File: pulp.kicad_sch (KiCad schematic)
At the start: 0 parts

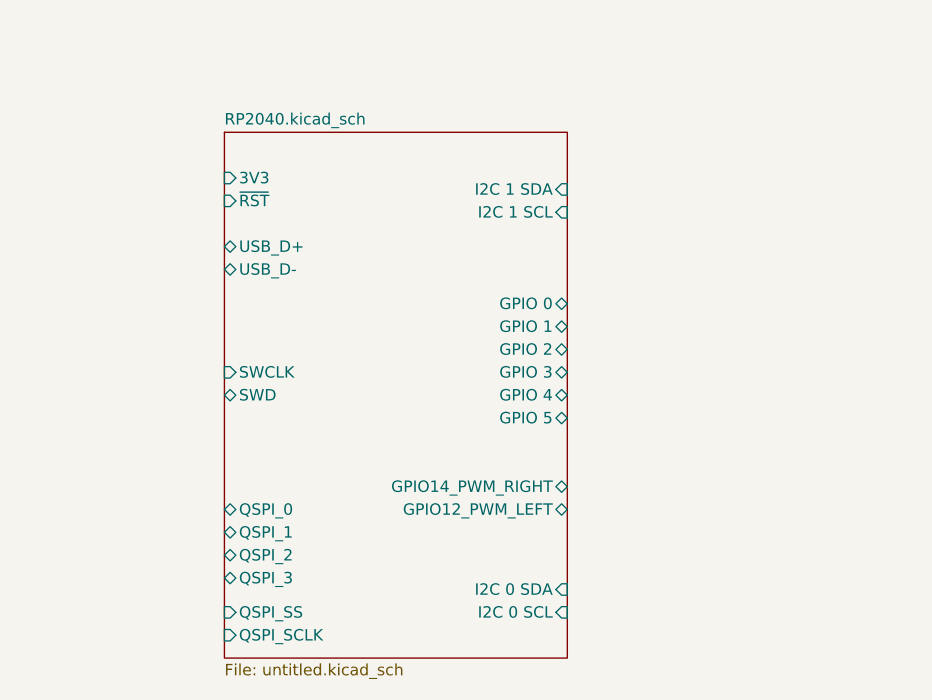
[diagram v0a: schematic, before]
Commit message: adds QMC5883L
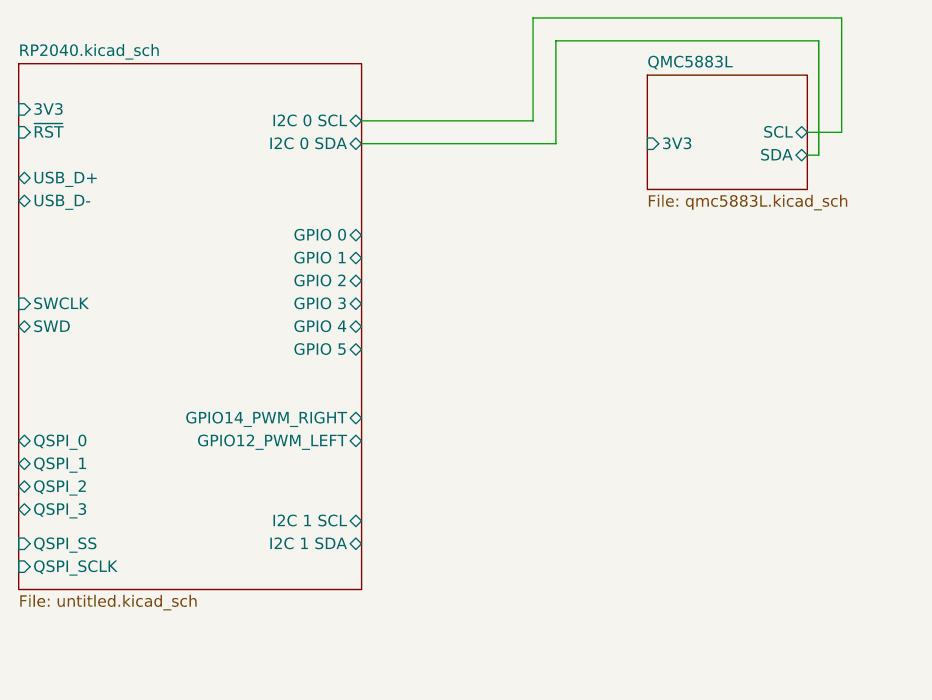
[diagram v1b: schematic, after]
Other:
- added sheet QMC5883L (qmc5883L.kicad_sch)
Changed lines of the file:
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@@
 (kicad_sch (version 20230121) (generator eeschema)
   (paper "A4")
-  (sheet (at 55.88 29.21) (size 38.1 58.42) (fields_autoplaced)
+  (wire (pts (xy 92.71 30.48) (xy 92.71 19.05))
+    (stroke (width 0) (type default))
+  )
+  (wire (pts (xy 121.92 31.75) (xy 120.65 31.75))
+    (stroke (width 0) (type default))
+  )
+  (wire (pts (xy 71.12 27.94) (xy 90.17 27.94))
+    (stroke (width 0) (type default))
+  )
+  (wire (pts (xy 121.92 19.05) (xy 121.92 31.75))
+    (stroke (width 0) (type default))
+  )
+  (wire (pts (xy 124.46 29.21) (xy 120.65 29.21))
+    (stroke (width 0) (type default))
+  )
+  (wire (pts (xy 90.17 27.94) (xy 90.17 16.51))
+    (stroke (width 0) (type default))
+  )
+  (wire (pts (xy 124.46 16.51) (xy 124.46 29.21))
+    (stroke (width 0) (type default))
+  )
+  (wire (pts (xy 90.17 16.51) (xy 124.46 16.51))
+    (stroke (width 0) (type default))
+  )
+  (wire (pts (xy 71.12 30.48) (xy 92.71 30.48))
+    (stroke (width 0) (type default))
+  )
+  (wire (pts (xy 92.71 19.05) (xy 121.92 19.05))
+    (stroke (width 0) (type default))
+  )
+  (sheet (at 33.02 21.59) (size 38.1 58.42) (fields_autoplaced)
     (stroke (width 0.1524) (type solid))
     (fill (color 0 0 0 0.0000))
-    (property "Sheetname" "RP2040.kicad_sch" (at 55.88 28.4984 0)
+    (property "Sheetname" "RP2040.kicad_sch" (at 33.02 20.8784 0)
       (effects (font (size 1.27 1.27)) (justify left bottom))
     )
-    (property "Sheetfile" "untitled.kicad_sch" (at 55.88 88.2146 0)
+    (property "Sheetfile" "untitled.kicad_sch" (at 33.02 80.5946 0)
       (effects (font (size 1.27 1.27)) (justify left top))
     )
-    (pin "3V3" input (at 55.88 34.29 180)
+    (pin "3V3" input (at 33.02 26.67 180)
       (effects (font (size 1.27 1.27)) (justify left))
     )
-    (pin "~{RST}" input (at 55.88 36.83 180)
+    (pin "~{RST}" input (at 33.02 29.21 180)
       (effects (font (size 1.27 1.27)) (justify left))
     )
-    (pin "SWD" bidirectional (at 55.88 58.42 180)
+    (pin "SWD" bidirectional (at 33.02 50.8 180)
       (effects (font (size 1.27 1.27)) (justify left))
     )
-    (pin "SWCLK" input (at 55.88 55.88 180)
+    (pin "SWCLK" input (at 33.02 48.26 180)
       (effects (font (size 1.27 1.27)) (justify left))
     )
-    (pin "QSPI_SCLK" input (at 55.88 85.09 180)
+    (pin "QSPI_SCLK" input (at 33.02 77.47 180)
       (effects (font (size 1.27 1.27)) (justify left))
     )
-    (pin "USB_D-" bidirectional (at 55.88 44.45 180)
+    (pin "USB_D-" bidirectional (at 33.02 36.83 180)
       (effects (font (size 1.27 1.27)) (justify left))
     )
-    (pin "QSPI_SS" input (at 55.88 82.55 180)
+    (pin "QSPI_SS" input (at 33.02 74.93 180)
       (effects (font (size 1.27 1.27)) (justify left))
     )
-    (pin "USB_D+" bidirectional (at 55.88 41.91 180)
+    (pin "USB_D+" bidirectional (at 33.02 34.29 180)
       (effects (font (size 1.27 1.27)) (justify left))
     )
-    (pin "QSPI_3" bidirectional (at 55.88 78.74 180)
+    (pin "QSPI_3" bidirectional (at 33.02 71.12 180)
       (effects (font (size 1.27 1.27)) (justify left))
     )
-    (pin "QSPI_2" bidirectional (at 55.88 76.2 180)
+    (pin "QSPI_2" bidirectional (at 33.02 68.58 180)
       (effects (font (size 1.27 1.27)) (justify left))
     )
-    (pin "QSPI_1" bidirectional (at 55.88 73.66 180)
+    (pin "QSPI_1" bidirectional (at 33.02 66.04 180)
       (effects (font (size 1.27 1.27)) (justify left))
     )
-    (pin "QSPI_0" bidirectional (at 55.88 71.12 180)
+    (pin "QSPI_0" bidirectional (at 33.02 63.5 180)
       (effects (font (size 1.27 1.27)) (justify left))
     )
-    (pin "I2C 1 SDA" input (at 93.98 35.56 0)
+    (pin "GPIO 4" bidirectional (at 71.12 50.8 0)
       (effects (font (size 1.27 1.27)) (justify right))
     )
-    (pin "I2C 1 SCL" input (at 93.98 38.1 0)
+    (pin "GPIO 1" bidirectional (at 71.12 43.18 0)
       (effects (font (size 1.27 1.27)) (justify right))
     )
-    (pin "I2C 0 SDA" input (at 93.98 80.01 0)
+    (pin "GPIO 2" bidirectional (at 71.12 45.72 0)
       (effects (font (size 1.27 1.27)) (justify right))
     )
-    (pin "I2C 0 SCL" input (at 93.98 82.55 0)
+    (pin "GPIO 3" bidirectional (at 71.12 48.26 0)
       (effects (font (size 1.27 1.27)) (justify right))
     )
-    (pin "GPIO 4" bidirectional (at 93.98 58.42 0)
+    (pin "GPIO 5" bidirectional (at 71.12 53.34 0)
       (effects (font (size 1.27 1.27)) (justify right))
     )
-    (pin "GPIO 1" bidirectional (at 93.98 50.8 0)
+    (pin "GPIO 0" bidirectional (at 71.12 40.64 0)
       (effects (font (size 1.27 1.27)) (justify right))
     )
-    (pin "GPIO 2" bidirectional (at 93.98 53.34 0)
+    (pin "GPIO14_PWM_RIGHT" bidirectional (at 71.12 60.96 0)
       (effects (font (size 1.27 1.27)) (justify right))
     )
-    (pin "GPIO 3" bidirectional (at 93.98 55.88 0)
+    (pin "GPIO12_PWM_LEFT" bidirectional (at 71.12 63.5 0)
       (effects (font (size 1.27 1.27)) (justify right))
     )
-    (pin "GPIO 5" bidirectional (at 93.98 60.96 0)
+    (pin "I2C 0 SCL" bidirectional (at 71.12 27.94 0)
       (effects (font (size 1.27 1.27)) (justify right))
     )
-    (pin "GPIO 0" bidirectional (at 93.98 48.26 0)
+    (pin "I2C 1 SDA" bidirectional (at 71.12 74.93 0)
       (effects (font (size 1.27 1.27)) (justify right))
     )
-    (pin "GPIO14_PWM_RIGHT" bidirectional (at 93.98 68.58 0)
+    (pin "I2C 0 SDA" bidirectional (at 71.12 30.48 0)
       (effects (font (size 1.27 1.27)) (justify right))
     )
-    (pin "GPIO12_PWM_LEFT" bidirectional (at 93.98 71.12 0)
+    (pin "I2C 1 SCL" bidirectional (at 71.12 72.39 0)
       (effects (font (size 1.27 1.27)) (justify right))
     )
@@
       )
     )
+  )
+  (sheet (at 102.87 22.86) (size 17.78 12.7) (fields_autoplaced)
+    (stroke (width 0.1524) (type solid))
+    (fill (color 0 0 0 0.0000))
+    (property "Sheetname" "QMC5883L" (at 102.87 22.1484 0)
+      (effects (font (size 1.27 1.27)) (justify left bottom))
+    )
+    (property "Sheetfile" "qmc5883L.kicad_sch" (at 102.87 36.1446 0)
+      (effects (font (size 1.27 1.27)) (justify left top))
+    )
+    (pin "3V3" input (at 102.87 30.48 180)
+      (effects (font (size 1.27 1.27)) (justify left))
+    )
+    (pin "SCL" bidirectional (at 120.65 29.21 0)
+      (effects (font (size 1.27 1.27)) (justify right))
+    )
+    (pin "SDA" bidirectional (at 120.65 31.75 0)
+      (effects (font (size 1.27 1.27)) (justify right))
+    )
+    (instances
+      (project "pulp"
+        (path "/1ed16f22-2fbd-4fb8-a593-4becb783d131" (page "3"))
+      )
+    )

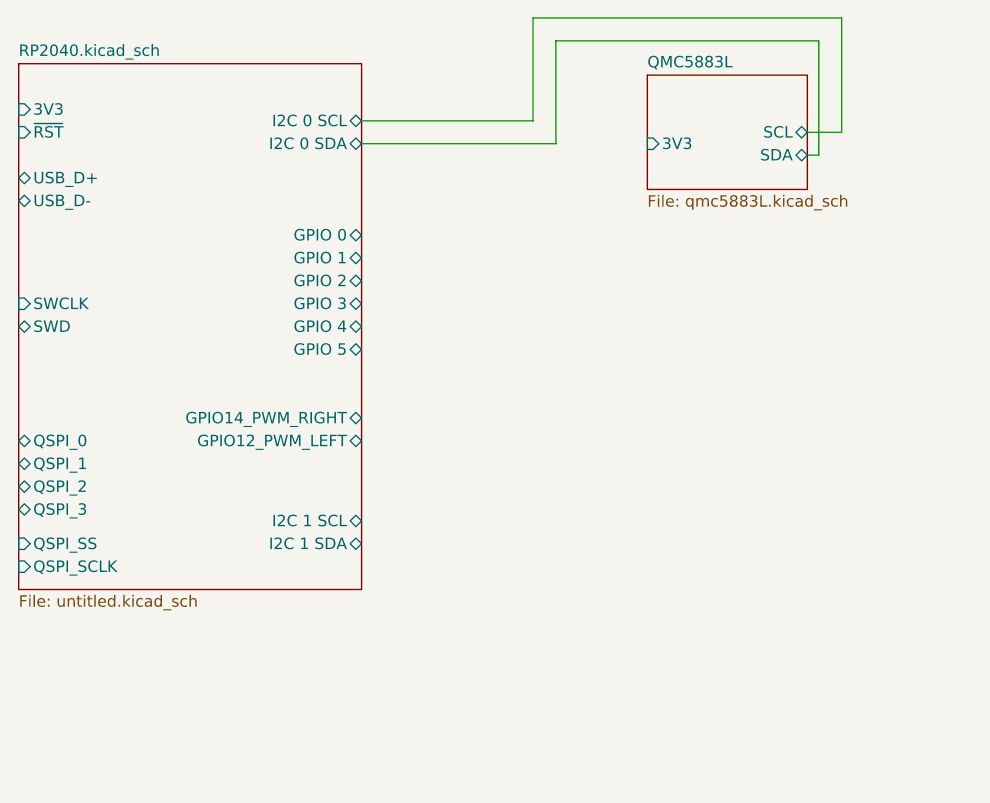
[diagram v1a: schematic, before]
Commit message: adds GNSS module
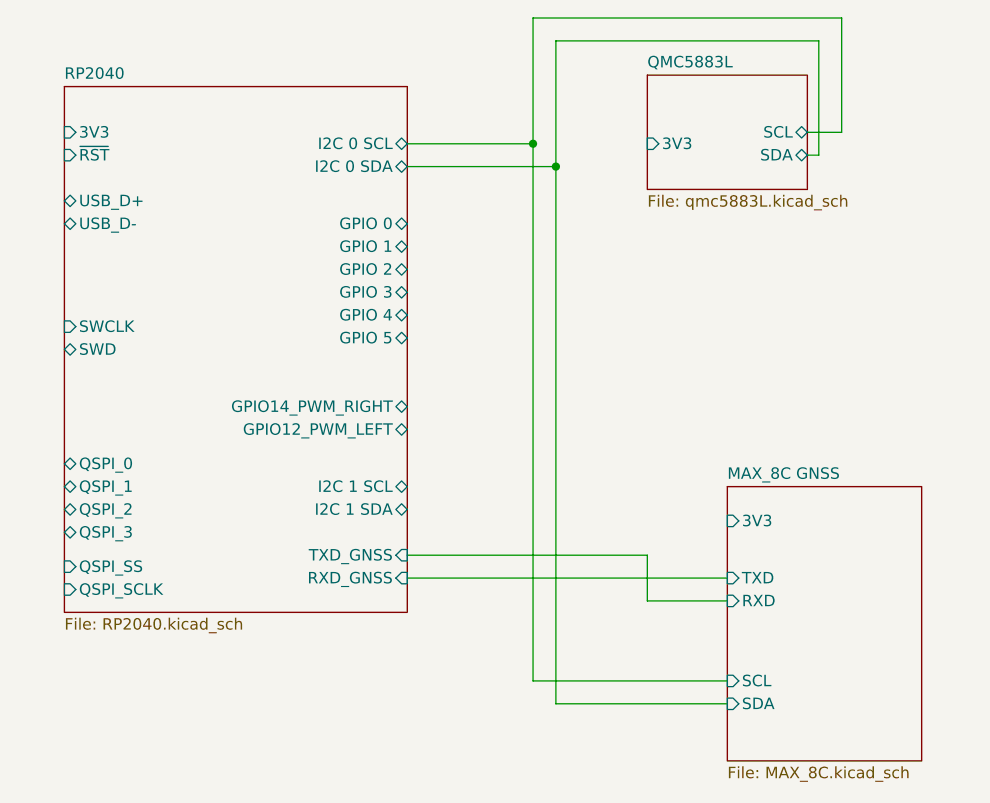
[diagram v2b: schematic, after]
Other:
- sheet RP2040.kicad_sch renamed RP2040
- added sheet MAX_8C GNSS (MAX_8C.kicad_sch)
- sheet RP2040: file untitled.kicad_sch -> RP2040.kicad_sch
- sheet RP2040 ports: added RXD_GNSS, TXD_GNSS; removed none
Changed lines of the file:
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@@
 (kicad_sch (version 20230121) (generator eeschema)
   (paper "A4")
-  (wire (pts (xy 92.71 30.48) (xy 92.71 19.05))
+  (junction (at 92.71 33.02) (diameter 0) (color 0 0 0 0)
+  )
+  (junction (at 90.17 30.48) (diameter 0) (color 0 0 0 0)
+  )
+  (wire (pts (xy 92.71 19.05) (xy 92.71 33.02))
     (stroke (width 0) (type default))
   )
@@
     (stroke (width 0) (type default))
   )
-  (wire (pts (xy 71.12 27.94) (xy 90.17 27.94))
+  (wire (pts (xy 90.17 16.51) (xy 90.17 30.48))
+    (stroke (width 0) (type default))
+  )
+  (wire (pts (xy 76.2 78.74) (xy 111.76 78.74))
+    (stroke (width 0) (type default))
+  )
+  (wire (pts (xy 92.71 92.71) (xy 111.76 92.71))
+    (stroke (width 0) (type default))
+  )
+  (wire (pts (xy 76.2 30.48) (xy 90.17 30.48))
+    (stroke (width 0) (type default))
+  )
+  (wire (pts (xy 92.71 33.02) (xy 92.71 92.71))
     (stroke (width 0) (type default))
   )
@@
     (stroke (width 0) (type default))
   )
-  (wire (pts (xy 90.17 27.94) (xy 90.17 16.51))
+  (wire (pts (xy 90.17 90.17) (xy 111.76 90.17))
     (stroke (width 0) (type default))
   )
@@
     (stroke (width 0) (type default))
   )
+  (wire (pts (xy 102.87 81.28) (xy 111.76 81.28))
+    (stroke (width 0) (type default))
+  )
+  (wire (pts (xy 76.2 76.2) (xy 102.87 76.2))
+    (stroke (width 0) (type default))
+  )
+  (wire (pts (xy 90.17 30.48) (xy 90.17 90.17))
+    (stroke (width 0) (type default))
+  )
   (wire (pts (xy 90.17 16.51) (xy 124.46 16.51))
     (stroke (width 0) (type default))
   )
-  (wire (pts (xy 71.12 30.48) (xy 92.71 30.48))
+  (wire (pts (xy 76.2 33.02) (xy 92.71 33.02))
+    (stroke (width 0) (type default))
+  )
+  (wire (pts (xy 102.87 76.2) (xy 102.87 81.28))
     (stroke (width 0) (type default))
   )
@@
     (stroke (width 0) (type default))
   )
-  (sheet (at 33.02 21.59) (size 38.1 58.42) (fields_autoplaced)
+  (sheet (at 38.1 24.13) (size 38.1 58.42) (fields_autoplaced)
     (stroke (width 0.1524) (type solid))
     (fill (color 0 0 0 0.0000))
-    (property "Sheetname" "RP2040.kicad_sch" (at 33.02 20.8784 0)
+    (property "Sheetname" "RP2040" (at 38.1 23.4184 0)
       (effects (font (size 1.27 1.27)) (justify left bottom))
     )
-    (property "Sheetfile" "untitled.kicad_sch" (at 33.02 80.5946 0)
+    (property "Sheetfile" "RP2040.kicad_sch" (at 38.1 83.1346 0)
       (effects (font (size 1.27 1.27)) (justify left top))
     )
-    (pin "3V3" input (at 33.02 26.67 180)
-      (effects (font (size 1.27 1.27)) (justify left))
-    )
-    (pin "~{RST}" input (at 33.02 29.21 180)
-      (effects (font (size 1.27 1.27)) (justify left))
-    )
-    (pin "SWD" bidirectional (at 33.02 50.8 180)
-      (effects (font (size 1.27 1.27)) (justify left))
-    )
-    (pin "SWCLK" input (at 33.02 48.26 180)
-      (effects (font (size 1.27 1.27)) (justify left))
-    )
-    (pin "QSPI_SCLK" input (at 33.02 77.47 180)
-      (effects (font (size 1.27 1.27)) (justify left))
-    )
-    (pin "USB_D-" bidirectional (at 33.02 36.83 180)
-      (effects (font (size 1.27 1.27)) (justify left))
-    )
-    (pin "QSPI_SS" input (at 33.02 74.93 180)
-      (effects (font (size 1.27 1.27)) (justify left))
-    )
-    (pin "USB_D+" bidirectional (at 33.02 34.29 180)
-      (effects (font (size 1.27 1.27)) (justify left))
-    )
-    (pin "QSPI_3" bidirectional (at 33.02 71.12 180)
-      (effects (font (size 1.27 1.27)) (justify left))
-    )
-    (pin "QSPI_2" bidirectional (at 33.02 68.58 180)
-      (effects (font (size 1.27 1.27)) (justify left))
-    )
-    (pin "QSPI_1" bidirectional (at 33.02 66.04 180)
-      (effects (font (size 1.27 1.27)) (justify left))
-    )
-    (pin "QSPI_0" bidirectional (at 33.02 63.5 180)
-      (effects (font (size 1.27 1.27)) (justify left))
-    )
-    (pin "GPIO 4" bidirectional (at 71.12 50.8 0)
-      (effects (font (size 1.27 1.27)) (justify right))
-    )
-    (pin "GPIO 1" bidirectional (at 71.12 43.18 0)
-      (effects (font (size 1.27 1.27)) (justify right))
-    )
-    (pin "GPIO 2" bidirectional (at 71.12 45.72 0)
-      (effects (font (size 1.27 1.27)) (justify right))
-    )
-    (pin "GPIO 3" bidirectional (at 71.12 48.26 0)
-      (effects (font (size 1.27 1.27)) (justify right))
-    )
-    (pin "GPIO 5" bidirectional (at 71.12 53.34 0)
-      (effects (font (size 1.27 1.27)) (justify right))
-    )
-    (pin "GPIO 0" bidirectional (at 71.12 40.64 0)
-      (effects (font (size 1.27 1.27)) (justify right))
-    )
-    (pin "GPIO14_PWM_RIGHT" bidirectional (at 71.12 60.96 0)
-      (effects (font (size 1.27 1.27)) (justify right))
-    )
-    (pin "GPIO12_PWM_LEFT" bidirectional (at 71.12 63.5 0)
-      (effects (font (size 1.27 1.27)) (justify right))
-    )
-    (pin "I2C 0 SCL" bidirectional (at 71.12 27.94 0)
-      (effects (font (size 1.27 1.27)) (justify right))
-    )
-    (pin "I2C 1 SDA" bidirectional (at 71.12 74.93 0)
-      (effects (font (size 1.27 1.27)) (justify right))
-    )
-    (pin "I2C 0 SDA" bidirectional (at 71.12 30.48 0)
-      (effects (font (size 1.27 1.27)) (justify right))
-    )
-    (pin "I2C 1 SCL" bidirectional (at 71.12 72.39 0)
+    (pin "3V3" input (at 38.1 29.21 180)
+      (effects (font (size 1.27 1.27)) (justify left))
+    )
+    (pin "~{RST}" input (at 38.1 31.75 180)
+      (effects (font (size 1.27 1.27)) (justify left))
+    )
+    (pin "SWD" bidirectional (at 38.1 53.34 180)
+      (effects (font (size 1.27 1.27)) (justify left))
+    )
+    (pin "SWCLK" input (at 38.1 50.8 180)
+      (effects (font (size 1.27 1.27)) (justify left))
+    )
+    (pin "QSPI_SCLK" input (at 38.1 80.01 180)
+      (effects (font (size 1.27 1.27)) (justify left))
+    )
+    (pin "USB_D-" bidirectional (at 38.1 39.37 180)
+      (effects (font (size 1.27 1.27)) (justify left))
+    )
+    (pin "QSPI_SS" input (at 38.1 77.47 180)
+      (effects (font (size 1.27 1.27)) (justify left))
+    )
+    (pin "USB_D+" bidirectional (at 38.1 36.83 180)
+      (effects (font (size 1.27 1.27)) (justify left))
+    )
+    (pin "QSPI_3" bidirectional (at 38.1 73.66 180)
+      (effects (font (size 1.27 1.27)) (justify left))
+    )
+    (pin "QSPI_2" bidirectional (at 38.1 71.12 180)
+      (effects (font (size 1.27 1.27)) (justify left))
+    )
+    (pin "QSPI_1" bidirectional (at 38.1 68.58 180)
+      (effects (font (size 1.27 1.27)) (justify left))
+    )
+    (pin "QSPI_0" bidirectional (at 38.1 66.04 180)
+      (effects (font (size 1.27 1.27)) (justify left))
+    )
+    (pin "GPIO 4" bidirectional (at 76.2 49.53 0)
+      (effects (font (size 1.27 1.27)) (justify right))
+    )
+    (pin "GPIO 1" bidirectional (at 76.2 41.91 0)
+      (effects (font (size 1.27 1.27)) (justify right))
+    )
+    (pin "GPIO 2" bidirectional (at 76.2 44.45 0)
+      (effects (font (size 1.27 1.27)) (justify right))
+    )
+    (pin "GPIO 3" bidirectional (at 76.2 46.99 0)
+      (effects (font (size 1.27 1.27)) (justify right))
+    )
+    (pin "GPIO 5" bidirectional (at 76.2 52.07 0)
+      (effects (font (size 1.27 1.27)) (justify right))
+    )
+    (pin "GPIO 0" bidirectional (at 76.2 39.37 0)
+      (effects (font (size 1.27 1.27)) (justify right))
+    )
+    (pin "GPIO14_PWM_RIGHT" bidirectional (at 76.2 59.69 0)
+      (effects (font (size 1.27 1.27)) (justify right))
+    )
+    (pin "GPIO12_PWM_LEFT" bidirectional (at 76.2 62.23 0)
+      (effects (font (size 1.27 1.27)) (justify right))
+    )
+    (pin "I2C 0 SCL" bidirectional (at 76.2 30.48 0)
+      (effects (font (size 1.27 1.27)) (justify right))
+    )
+    (pin "I2C 1 SDA" bidirectional (at 76.2 71.12 0)
+      (effects (font (size 1.27 1.27)) (justify right))
+    )
+    (pin "I2C 0 SDA" bidirectional (at 76.2 33.02 0)
+      (effects (font (size 1.27 1.27)) (justify right))
+    )
+    (pin "I2C 1 SCL" bidirectional (at 76.2 68.58 0)
+      (effects (font (size 1.27 1.27)) (justify right))
+    )
+    (pin "RXD_GNSS" input (at 76.2 78.74 0)
+      (effects (font (size 1.27 1.27)) (justify right))
+    )
+    (pin "TXD_GNSS" input (at 76.2 76.2 0)
       (effects (font (size 1.27 1.27)) (justify right))
     )
@@
       )
     )
+  )
+  (sheet (at 111.76 68.58) (size 21.59 30.48) (fields_autoplaced)
+    (stroke (width 0.1524) (type solid))
+    (fill (color 0 0 0 0.0000))
+    (property "Sheetname" "MAX_8C GNSS" (at 111.76 67.8684 0)
+      (effects (font (size 1.27 1.27)) (justify left bottom))
+    )
+    (property "Sheetfile" "MAX_8C.kicad_sch" (at 111.76 99.6446 0)
+      (effects (font (size 1.27 1.27)) (justify left top))
+    )
+    (pin "3V3" input (at 111.76 72.39 180)
+      (effects (font (size 1.27 1.27)) (justify left))
+    )
+    (pin "RXD" input (at 111.76 81.28 180)
+      (effects (font (size 1.27 1.27)) (justify left))
+    )
+    (pin "TXD" input (at 111.76 78.74 180)
+      (effects (font (size 1.27 1.27)) (justify left))
+    )
+    (pin "SDA" input (at 111.76 92.71 180)
+      (effects (font (size 1.27 1.27)) (justify left))
+    )
+    (pin "SCL" input (at 111.76 90.17 180)
+      (effects (font (size 1.27 1.27)) (justify left))
+    )
+    (instances
+      (project "pulp"
+        (path "/1ed16f22-2fbd-4fb8-a593-4becb783d131" (page "4"))
+      )
+    )
